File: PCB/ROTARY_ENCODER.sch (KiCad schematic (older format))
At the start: 4 parts, among them SW4 ENCODER

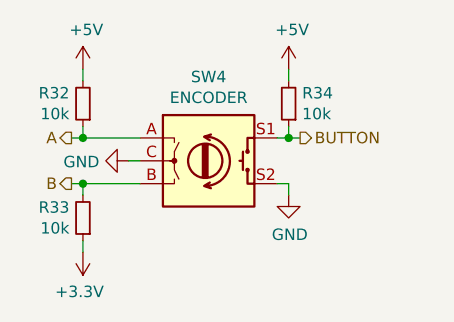
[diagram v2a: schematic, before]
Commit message: Added remaining test points
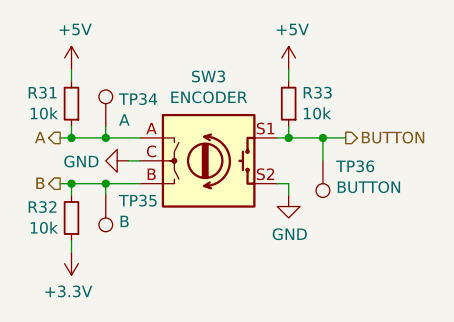
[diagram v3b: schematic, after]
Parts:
- added TP34: A, symbol Connector:TestPoint
- added TP35: B, symbol Connector:TestPoint
- added TP36: BUTTON, symbol Connector:TestPoint
- renumbered R32 to R31, R33 to R32, R34 to R33, SW4 to SW3
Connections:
- net A: now also TP34.1
- net B: now also TP35.1
- net BUTTON: now also TP36.1
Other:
- moved on the sheet: R31, R32
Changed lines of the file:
@@
 $EndDescr
 $Comp
-L Device:Rotary_Encoder_Switch SW4
+L Device:Rotary_Encoder_Switch SW3
 U 1 1 5E8BF4A3
 P 5800 4050
-F 0 "SW4" H 5800 4417 50  0000 C CNN
+F 0 "SW3" H 5800 4417 50  0000 C CNN
 F 1 "ENCODER" H 5800 4326 50  0000 C CNN
 F 2 "" H 5650 4210 50  0001 C CNN
@@
 $EndComp
 $Comp
-L Device:R_Small R32
+L Device:R_Small R31
 U 1 1 5E8BFE00
-P 5250 3800
-F 0 "R32" H 5309 3754 50  0000 L CNN
-F 1 "10k" H 5309 3845 50  0000 L CNN
-F 2 "" H 5250 3800 50  0001 C CNN
-F 3 "" H 5250 3800 50  0001 C CNN
-	1    5250 3800
+P 5200 3800
+F 0 "R31" H 5259 3754 50  0000 L CNN
+F 1 "10k" H 5259 3845 50  0000 L CNN
+F 2 "" H 5200 3800 50  0001 C CNN
+F 3 "" H 5200 3800 50  0001 C CNN
+	1    5200 3800
 	-1   0    0    1
 $EndComp
 $Comp
-L Device:R_Small R33
+L Device:R_Small R32
 U 1 1 5E8C002C
-P 5250 4300
-F 0 "R33" H 5309 4254 50  0000 L CNN
-F 1 "10k" H 5309 4345 50  0000 L CNN
-F 2 "" H 5250 4300 50  0001 C CNN
-F 3 "" H 5250 4300 50  0001 C CNN
-	1    5250 4300
+P 5200 4300
+F 0 "R32" H 5259 4254 50  0000 L CNN
+F 1 "10k" H 5259 4345 50  0000 L CNN
+F 2 "" H 5200 4300 50  0001 C CNN
+F 3 "" H 5200 4300 50  0001 C CNN
+	1    5200 4300
 	-1   0    0    1
 $EndComp
 Wire Wire Line
-	5500 3950 5250 3950
+	5500 3950 5350 3950
 Wire Wire Line
-	5250 3950 5250 3900
+	5200 3950 5200 3900
 Wire Wire Line
-	5250 3650 5250 3700
-Text HLabel 5200 3950 0    50   Output ~ 0
+	5200 3650 5200 3700
+Text HLabel 5150 3950 0    50   Output ~ 0
 A
 Wire Wire Line
-	5200 3950 5250 3950
-Connection ~ 5250 3950
-Text HLabel 5200 4150 0    50   Output ~ 0
+	5150 3950 5200 3950
+Connection ~ 5200 3950
+Text HLabel 5150 4150 0    50   Output ~ 0
 B
 $Comp
-L power:GND #PWR0131
+L power:GND #PWR0128
 U 1 1 5E8C2AF2
 P 5450 4050
-F 0 "#PWR0131" H 5450 3800 50  0001 C CNN
+F 0 "#PWR0128" H 5450 3800 50  0001 C CNN
 F 1 "GND" V 5455 3922 50  0000 R CNN
 F 2 "" H 5450 4050 50  0001 C CNN
@@
 	5450 4050 5500 4050
 Wire Wire Line
-	5250 4200 5250 4150
+	5200 4200 5200 4150
 Wire Wire Line
-	5250 4150 5500 4150
+	5200 4150 5350 4150
 $Comp
-L power:+3.3V #PWR0130
+L power:+3.3V #PWR0127
 U 1 1 5E8C4253
-P 5250 4450
-F 0 "#PWR0130" H 5250 4300 50  0001 C CNN
-F 1 "+3.3V" H 5265 4623 50  0000 C CNN
-F 2 "" H 5250 4450 50  0001 C CNN
-F 3 "" H 5250 4450 50  0001 C CNN
-	1    5250 4450
+P 5200 4450
+F 0 "#PWR0127" H 5200 4300 50  0001 C CNN
+F 1 "+3.3V" H 5215 4623 50  0000 C CNN
+F 2 "" H 5200 4450 50  0001 C CNN
+F 3 "" H 5200 4450 50  0001 C CNN
+	1    5200 4450
 	-1   0    0    1
 $EndComp
 Wire Wire Line
-	5250 4400 5250 4450
+	5200 4400 5200 4450
 Wire Wire Line
-	5200 4150 5250 4150
-Connection ~ 5250 4150
+	5150 4150 5200 4150
+Connection ~ 5200 4150
 $Comp
-L Device:R_Small R34
+L Device:R_Small R33
 U 1 1 5E8C58DC
 P 6150 3800
-F 0 "R34" H 6091 3754 50  0000 R CNN
+F 0 "R33" H 6091 3754 50  0000 R CNN
 F 1 "10k" H 6091 3845 50  0000 R CNN
 F 2 "" H 6150 3800 50  0001 C CNN
@@
 	6150 3650 6150 3700
 $Comp
-L power:GND #PWR0133
+L power:GND #PWR0130
 U 1 1 5E8C6704
 P 6150 4200
-F 0 "#PWR0133" H 6150 3950 50  0001 C CNN
+F 0 "#PWR0130" H 6150 3950 50  0001 C CNN
 F 1 "GND" H 6155 4027 50  0000 C CNN
 F 2 "" H 6150 4200 50  0001 C CNN
@@
 Wire Wire Line
 	6150 4150 6150 4200
-Text HLabel 6200 3950 2    50   Output ~ 0
+Text HLabel 6400 3950 2    50   Output ~ 0
 BUTTON
 Wire Wire Line
-	6200 3950 6150 3950
+	6400 3950 6300 3950
 Connection ~ 6150 3950
 $Comp
@@
 P 6150 3650
 AR Path="/5E8A6686/5E91E86F" Ref="#PWR?"  Part="1"
-AR Path="/5E8BEE14/5E91E86F" Ref="#PWR0132"  Part="1"
-F 0 "#PWR0132" H 6150 3500 50  0001 C CNN
+AR Path="/5E8BEE14/5E91E86F" Ref="#PWR0129"  Part="1"
+F 0 "#PWR0129" H 6150 3500 50  0001 C CNN
 F 1 "+5V" H 6165 3823 50  0000 C CNN
 F 2 "" H 6150 3650 50  0001 C CNN
@@
 L power:+5V #PWR?
 U 1 1 5E91E997
-P 5250 3650
+P 5200 3650
 AR Path="/5E8A6686/5E91E997" Ref="#PWR?"  Part="1"
-AR Path="/5E8BEE14/5E91E997" Ref="#PWR0129"  Part="1"
-F 0 "#PWR0129" H 5250 3500 50  0001 C CNN
-F 1 "+5V" H 5265 3823 50  0000 C CNN
-F 2 "" H 5250 3650 50  0001 C CNN
-F 3 "" H 5250 3650 50  0001 C CNN
-	1    5250 3650
+AR Path="/5E8BEE14/5E91E997" Ref="#PWR0126"  Part="1"
+F 0 "#PWR0126" H 5200 3500 50  0001 C CNN
+F 1 "+5V" H 5215 3823 50  0000 C CNN
+F 2 "" H 5200 3650 50  0001 C CNN
+F 3 "" H 5200 3650 50  0001 C CNN
+	1    5200 3650
 	1    0    0    -1
 $EndComp
+$Comp
+L Connector:TestPoint TP?
+U 1 1 5E9C5BE3
+P 5350 4200
+AR Path="/5E9C5BE3" Ref="TP?"  Part="1"
+AR Path="/5E8BEE14/5E9C5BE3" Ref="TP35"  Part="1"
+F 0 "TP35" H 5292 4226 50  0000 R CNN
+F 1 "B" H 5292 4317 50  0000 R CNN
+F 2 "" H 5550 4200 50  0001 C CNN
+F 3 "~" H 5550 4200 50  0001 C CNN
+	1    5350 4200
+	-1   0    0    1
+$EndComp
+$Comp
+L Connector:TestPoint TP?
+U 1 1 5E9C5E1B
+P 5350 3900
+AR Path="/5E9C5E1B" Ref="TP?"  Part="1"
+AR Path="/5E8BEE14/5E9C5E1B" Ref="TP34"  Part="1"
+F 0 "TP34" H 5408 4018 50  0000 L CNN
+F 1 "A" H 5408 3927 50  0000 L CNN
+F 2 "" H 5550 3900 50  0001 C CNN
+F 3 "~" H 5550 3900 50  0001 C CNN
+	1    5350 3900
+	1    0    0    -1
+$EndComp
+Wire Wire Line
+	5350 3900 5350 3950
+Connection ~ 5350 3950
+Wire Wire Line
+	5350 3950 5200 3950
+Wire Wire Line
+	5350 4200 5350 4150
+Connection ~ 5350 4150
+Wire Wire Line
+	5350 4150 5500 4150
+$Comp
+L Connector:TestPoint TP?
+U 1 1 5E9CAECA
+P 6300 4050
+AR Path="/5E9CAECA" Ref="TP?"  Part="1"
+AR Path="/5E8BEE14/5E9CAECA" Ref="TP36"  Part="1"
+F 0 "TP36" H 6242 4076 50  0000 R CNN
+F 1 "BUTTON" H 6242 4167 50  0000 R CNN
+F 2 "" H 6500 4050 50  0001 C CNN
+F 3 "~" H 6500 4050 50  0001 C CNN
+	1    6300 4050
+	-1   0    0    1
+$EndComp
+Wire Wire Line
+	6300 4050 6300 3950
+Connection ~ 6300 3950
+Wire Wire Line
+	6300 3950 6150 3950
 $EndSCHEMATC

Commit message: Added majority footprints
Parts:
- R31, R32, R33: footprint (none) -> Resistor_SMD:R_0603_1608Metric
- SW3: footprint (none) -> Rotary_Encoder:RotaryEncoder_Alps_EC11E-Switch_Vertical_H20mm
- TP34, TP35, TP36: footprint (none) -> custom:TestPoint_Pad_D1.5mm
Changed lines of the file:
@@
 F 0 "SW3" H 5800 4417 50  0000 C CNN
 F 1 "ENCODER" H 5800 4326 50  0000 C CNN
-F 2 "" H 5650 4210 50  0001 C CNN
+F 2 "Rotary_Encoder:RotaryEncoder_Alps_EC11E-Switch_Vertical_H20mm" H 5650 4210 50  0001 C CNN
 F 3 "" H 5800 4310 50  0001 C CNN
 	1    5800 4050
@@
 F 0 "R31" H 5259 3754 50  0000 L CNN
 F 1 "10k" H 5259 3845 50  0000 L CNN
-F 2 "" H 5200 3800 50  0001 C CNN
+F 2 "Resistor_SMD:R_0603_1608Metric" H 5200 3800 50  0001 C CNN
 F 3 "" H 5200 3800 50  0001 C CNN
 	1    5200 3800
@@
 F 0 "R32" H 5259 4254 50  0000 L CNN
 F 1 "10k" H 5259 4345 50  0000 L CNN
-F 2 "" H 5200 4300 50  0001 C CNN
+F 2 "Resistor_SMD:R_0603_1608Metric" H 5200 4300 50  0001 C CNN
 F 3 "" H 5200 4300 50  0001 C CNN
 	1    5200 4300
@@
 F 0 "R33" H 6091 3754 50  0000 R CNN
 F 1 "10k" H 6091 3845 50  0000 R CNN
-F 2 "" H 6150 3800 50  0001 C CNN
+F 2 "Resistor_SMD:R_0603_1608Metric" H 6150 3800 50  0001 C CNN
 F 3 "" H 6150 3800 50  0001 C CNN
 	1    6150 3800
@@
 F 0 "TP35" H 5292 4226 50  0000 R CNN
 F 1 "B" H 5292 4317 50  0000 R CNN
-F 2 "" H 5550 4200 50  0001 C CNN
+F 2 "custom:TestPoint_Pad_D1.5mm" H 5550 4200 50  0001 C CNN
 F 3 "~" H 5550 4200 50  0001 C CNN
 	1    5350 4200
@@
 F 0 "TP34" H 5408 4018 50  0000 L CNN
 F 1 "A" H 5408 3927 50  0000 L CNN
-F 2 "" H 5550 3900 50  0001 C CNN
+F 2 "custom:TestPoint_Pad_D1.5mm" H 5550 3900 50  0001 C CNN
 F 3 "~" H 5550 3900 50  0001 C CNN
 	1    5350 3900
@@
 F 0 "TP36" H 6242 4076 50  0000 R CNN
 F 1 "BUTTON" H 6242 4167 50  0000 R CNN
-F 2 "" H 6500 4050 50  0001 C CNN
+F 2 "custom:TestPoint_Pad_D1.5mm" H 6500 4050 50  0001 C CNN
 F 3 "~" H 6500 4050 50  0001 C CNN
 	1    6300 4050

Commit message: Added Rotary encoder MPN and datasheet
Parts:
- SW3: footprint Rotary_Encoder:RotaryEncoder_Alps_EC11E-Switch_Vertical_H20mm -> Rotary_Encoder:RotaryEncoder_Alps_EC12E-Switch_Vertical_H20mm; MPN (none) -> EN12-HS22AF20
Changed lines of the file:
@@
 F 0 "SW3" H 5800 4417 50  0000 C CNN
 F 1 "ENCODER" H 5800 4326 50  0000 C CNN
-F 2 "Rotary_Encoder:RotaryEncoder_Alps_EC11E-Switch_Vertical_H20mm" H 5650 4210 50  0001 C CNN
-F 3 "" H 5800 4310 50  0001 C CNN
+F 2 "Rotary_Encoder:RotaryEncoder_Alps_EC12E-Switch_Vertical_H20mm" H 5650 4210 50  0001 C CNN
+F 3 "https://www.ttelectronics.com/TTElectronics/media/ProductFiles/Encoders/Datasheets/EN12.pdf" H 5800 4310 50  0001 C CNN
+F 4 "EN12-HS22AF20" H 5800 4050 50  0001 C CNN "MPN"
 	1    5800 4050
 	1    0    0    -1
